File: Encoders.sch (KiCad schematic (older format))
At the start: 32 parts

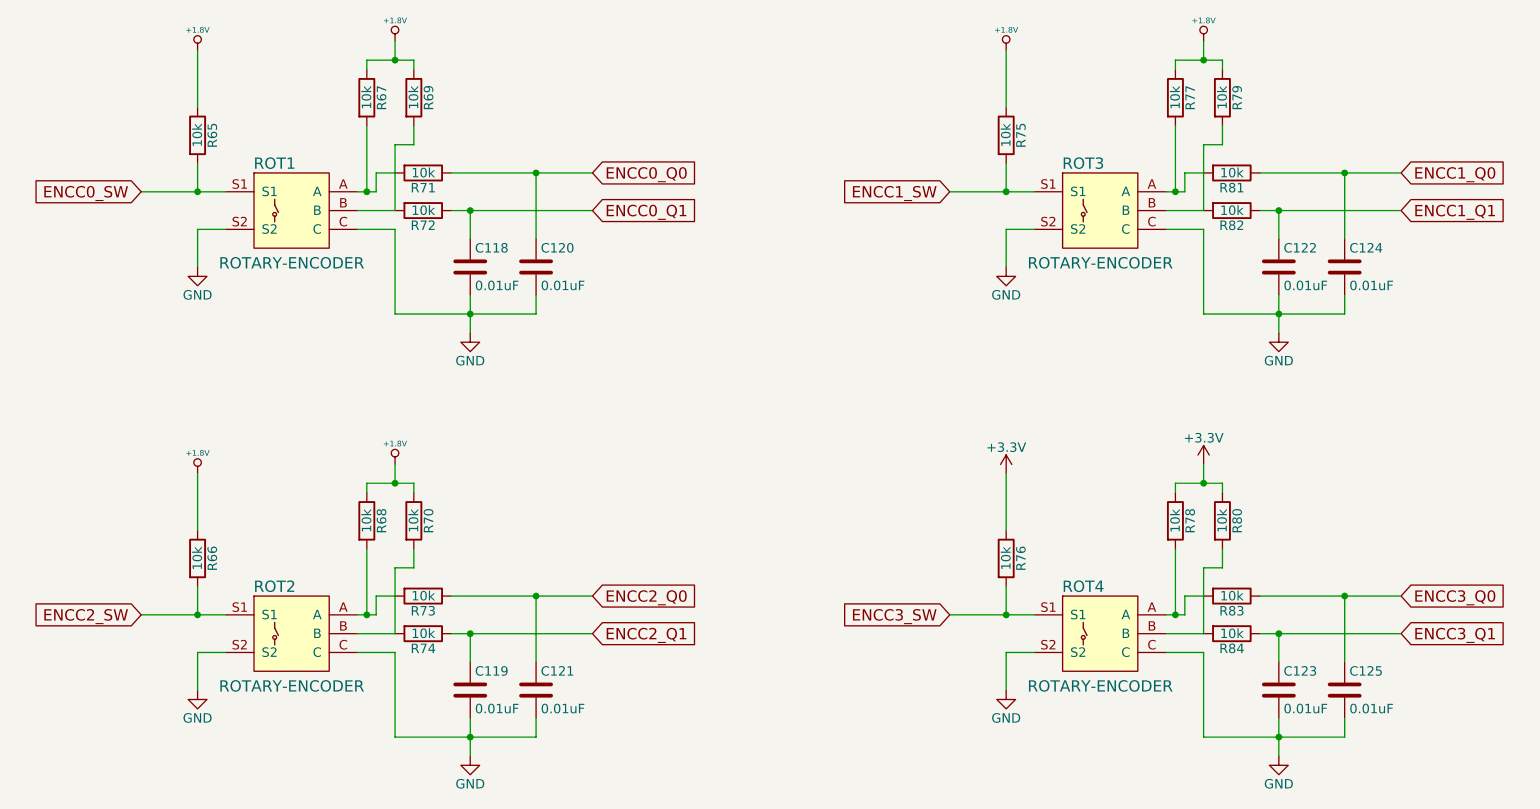
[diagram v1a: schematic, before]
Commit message: started PCBnew trivial connections and BGA interface, shuffled some net connections, etc.
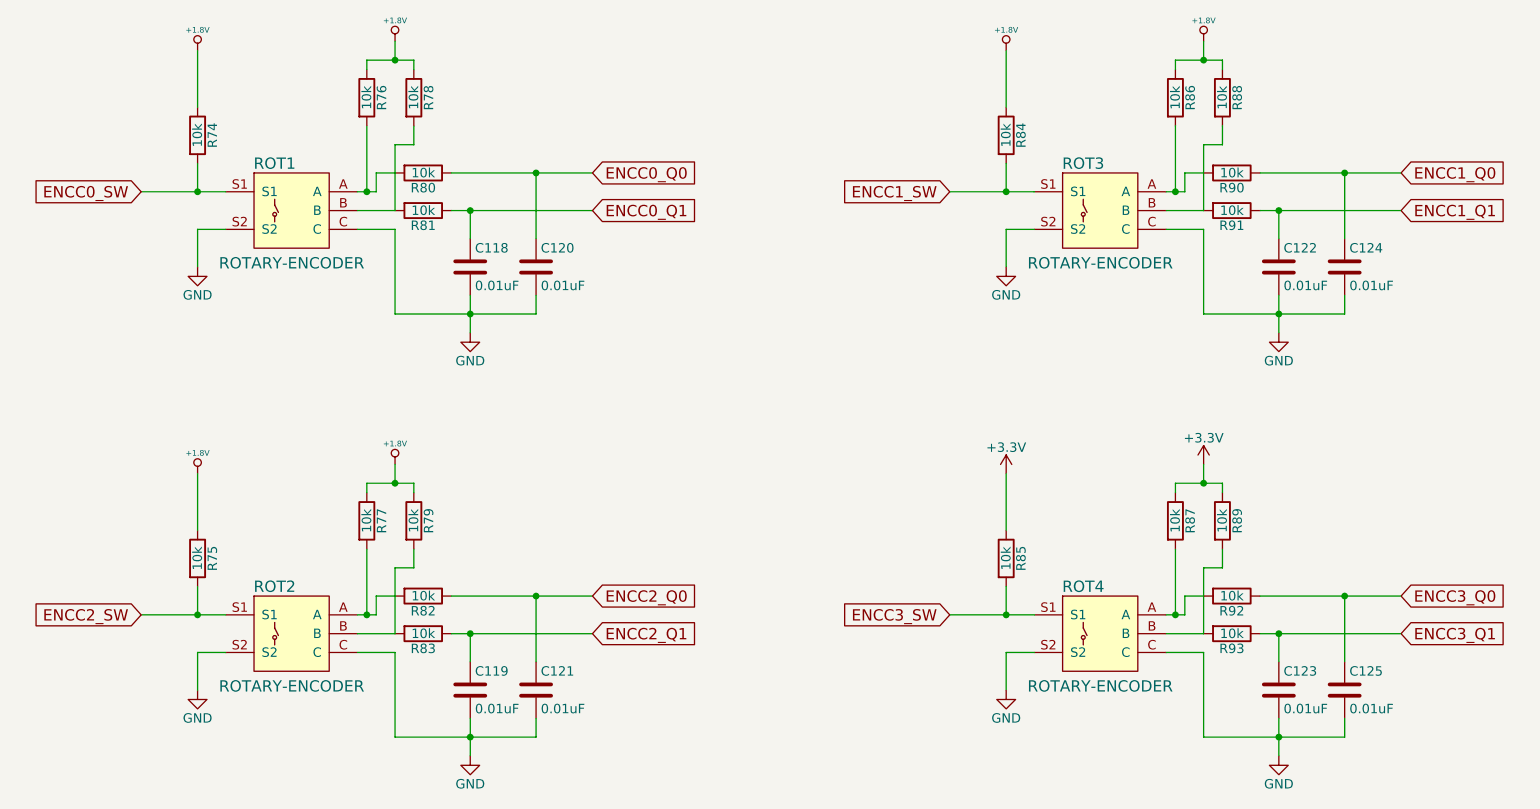
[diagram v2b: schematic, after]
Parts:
- renumbered R65 to R74, R66 to R75, R67 to R76, R68 to R77, R69 to R78, R70 to R79, R71 to R80, R72 to R81, R73 to R82, R74 to R83, R75 to R84, R76 to R85, R77 to R86, R78 to R87, R79 to R88, R80 to R89, R81 to R90, R82 to R91, R83 to R92, R84 to R93
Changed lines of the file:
@@
 LIBS:JACK_TRS_5PINS
 LIBS:MEMSMIC
+LIBS:illuminatedswitch
 EELAYER 25 0
 EELAYER END
@@
 $EndComp
 $Comp
-L R R72
+L R R81
 U 1 1 586C395E
 P 4150 2600
-F 0 "R72" V 4230 2600 50  0000 C CNN
+F 0 "R81" V 4230 2600 50  0000 C CNN
 F 1 "10k" V 4150 2600 50  0000 C CNN
 F 2 "Resistors_SMD:R_1206" V 4080 2600 50  0001 C CNN
@@
 $EndComp
 $Comp
-L R R71
+L R R80
 U 1 1 586C39C5
 P 4150 2400
-F 0 "R71" V 4230 2400 50  0000 C CNN
+F 0 "R80" V 4230 2400 50  0000 C CNN
 F 1 "10k" V 4150 2400 50  0000 C CNN
 F 2 "Resistors_SMD:R_1206" V 4080 2400 50  0001 C CNN
@@
 	4750 2400 4750 2750
 $Comp
-L R R67
+L R R76
 U 1 1 586C3A50
 P 3850 2000
-F 0 "R67" V 3930 2000 50  0000 C CNN
+F 0 "R76" V 3930 2000 50  0000 C CNN
 F 1 "10k" V 3850 2000 50  0000 C CNN
 F 2 "Resistors_SMD:R_1206" V 3780 2000 50  0001 C CNN
@@
 $EndComp
 $Comp
-L R R69
+L R R78
 U 1 1 586C3A87
 P 4100 2000
-F 0 "R69" V 4180 2000 50  0000 C CNN
+F 0 "R78" V 4180 2000 50  0000 C CNN
 F 1 "10k" V 4100 2000 50  0000 C CNN
 F 2 "Resistors_SMD:R_1206" V 4030 2000 50  0001 C CNN
@@
 Connection ~ 4000 1800
 $Comp
-L +1.8V #PWR0138
+L +1.8V #PWR0145
 U 1 1 586C41F4
 P 4000 1700
-F 0 "#PWR0138" H 4000 1840 20  0001 C CNN
+F 0 "#PWR0145" H 4000 1840 20  0001 C CNN
 F 1 "+1.8V" H 4000 1810 30  0000 C CNN
 F 2 "" H 4000 1700 60  0001 C CNN
@@
 $EndComp
 $Comp
-L GND #PWR0139
+L GND #PWR0146
 U 1 1 586C4216
 P 4400 3250
-F 0 "#PWR0139" H 4400 3000 50  0001 C CNN
+F 0 "#PWR0146" H 4400 3000 50  0001 C CNN
 F 1 "GND" H 4400 3100 50  0000 C CNN
 F 2 "" H 4400 3250 50  0000 C CNN
@@
 $EndComp
 $Comp
-L R R65
+L R R74
 U 1 1 586C42C6
 P 2950 2200
-F 0 "R65" V 3030 2200 50  0000 C CNN
+F 0 "R74" V 3030 2200 50  0000 C CNN
 F 1 "10k" V 2950 2200 50  0000 C CNN
 F 2 "Resistors_SMD:R_1206" V 2880 2200 50  0001 C CNN
@@
 	2950 2700 2950 2900
 $Comp
-L GND #PWR0140
+L GND #PWR0147
 U 1 1 586C437C
 P 2950 2900
-F 0 "#PWR0140" H 2950 2650 50  0001 C CNN
+F 0 "#PWR0147" H 2950 2650 50  0001 C CNN
 F 1 "GND" H 2950 2750 50  0000 C CNN
 F 2 "" H 2950 2900 50  0000 C CNN
@@
 $EndComp
 $Comp
-L +1.8V #PWR0141
+L +1.8V #PWR0148
 U 1 1 586C43A0
 P 2950 1750
-F 0 "#PWR0141" H 2950 1890 20  0001 C CNN
+F 0 "#PWR0148" H 2950 1890 20  0001 C CNN
 F 1 "+1.8V" H 2950 1860 30  0000 C CNN
 F 2 "" H 2950 1750 60  0001 C CNN
@@
 $EndComp
 $Comp
-L R R82
+L R R91
 U 1 1 586C5704
 P 8450 2600
-F 0 "R82" V 8530 2600 50  0000 C CNN
+F 0 "R91" V 8530 2600 50  0000 C CNN
 F 1 "10k" V 8450 2600 50  0000 C CNN
 F 2 "Resistors_SMD:R_1206" V 8380 2600 50  0001 C CNN
@@
 $EndComp
 $Comp
-L R R81
+L R R90
 U 1 1 586C570A
 P 8450 2400
-F 0 "R81" V 8530 2400 50  0000 C CNN
+F 0 "R90" V 8530 2400 50  0000 C CNN
 F 1 "10k" V 8450 2400 50  0000 C CNN
 F 2 "Resistors_SMD:R_1206" V 8380 2400 50  0001 C CNN
@@
 	9050 2400 9050 2750
 $Comp
-L R R77
+L R R86
 U 1 1 586C5718
 P 8150 2000
-F 0 "R77" V 8230 2000 50  0000 C CNN
+F 0 "R86" V 8230 2000 50  0000 C CNN
 F 1 "10k" V 8150 2000 50  0000 C CNN
 F 2 "Resistors_SMD:R_1206" V 8080 2000 50  0001 C CNN
@@
 $EndComp
 $Comp
-L R R79
+L R R88
 U 1 1 586C571E
 P 8400 2000
-F 0 "R79" V 8480 2000 50  0000 C CNN
+F 0 "R88" V 8480 2000 50  0000 C CNN
 F 1 "10k" V 8400 2000 50  0000 C CNN
 F 2 "Resistors_SMD:R_1206" V 8330 2000 50  0001 C CNN
@@
 Connection ~ 8300 1800
 $Comp
-L +1.8V #PWR0142
+L +1.8V #PWR0149
 U 1 1 586C5734
 P 8300 1700
-F 0 "#PWR0142" H 8300 1840 20  0001 C CNN
+F 0 "#PWR0149" H 8300 1840 20  0001 C CNN
 F 1 "+1.8V" H 8300 1810 30  0000 C CNN
 F 2 "" H 8300 1700 60  0001 C CNN
@@
 $EndComp
 $Comp
-L GND #PWR0143
+L GND #PWR0150
 U 1 1 586C573A
 P 8700 3250
-F 0 "#PWR0143" H 8700 3000 50  0001 C CNN
+F 0 "#PWR0150" H 8700 3000 50  0001 C CNN
 F 1 "GND" H 8700 3100 50  0000 C CNN
 F 2 "" H 8700 3250 50  0000 C CNN
@@
 $EndComp
 $Comp
-L R R75
+L R R84
 U 1 1 586C5740
 P 7250 2200
-F 0 "R75" V 7330 2200 50  0000 C CNN
+F 0 "R84" V 7330 2200 50  0000 C CNN
 F 1 "10k" V 7250 2200 50  0000 C CNN
 F 2 "Resistors_SMD:R_1206" V 7180 2200 50  0001 C CNN
@@
 	7250 2700 7250 2900
 $Comp
-L GND #PWR0144
+L GND #PWR0151
 U 1 1 586C5748
 P 7250 2900
-F 0 "#PWR0144" H 7250 2650 50  0001 C CNN
+F 0 "#PWR0151" H 7250 2650 50  0001 C CNN
 F 1 "GND" H 7250 2750 50  0000 C CNN
 F 2 "" H 7250 2900 50  0000 C CNN
@@
 $EndComp
 $Comp
-L +1.8V #PWR0145
+L +1.8V #PWR0152
 U 1 1 586C574E
 P 7250 1750
-F 0 "#PWR0145" H 7250 1890 20  0001 C CNN
+F 0 "#PWR0152" H 7250 1890 20  0001 C CNN
 F 1 "+1.8V" H 7250 1860 30  0000 C CNN
 F 2 "" H 7250 1750 60  0001 C CNN
@@
 $EndComp
 $Comp
-L R R74
+L R R83
 U 1 1 586C5B4F
 P 4150 4850
-F 0 "R74" V 4230 4850 50  0000 C CNN
+F 0 "R83" V 4230 4850 50  0000 C CNN
 F 1 "10k" V 4150 4850 50  0000 C CNN
 F 2 "Resistors_SMD:R_1206" V 4080 4850 50  0001 C CNN
@@
 $EndComp
 $Comp
-L R R73
+L R R82
 U 1 1 586C5B55
 P 4150 4650
-F 0 "R73" V 4230 4650 50  0000 C CNN
+F 0 "R82" V 4230 4650 50  0000 C CNN
 F 1 "10k" V 4150 4650 50  0000 C CNN
 F 2 "Resistors_SMD:R_1206" V 4080 4650 50  0001 C CNN
@@
 	4750 4650 4750 5000
 $Comp
-L R R68
+L R R77
 U 1 1 586C5B63
 P 3850 4250
-F 0 "R68" V 3930 4250 50  0000 C CNN
+F 0 "R77" V 3930 4250 50  0000 C CNN
 F 1 "10k" V 3850 4250 50  0000 C CNN
 F 2 "Resistors_SMD:R_1206" V 3780 4250 50  0001 C CNN
@@
 $EndComp
 $Comp
-L R R70
+L R R79
 U 1 1 586C5B69
 P 4100 4250
-F 0 "R70" V 4180 4250 50  0000 C CNN
+F 0 "R79" V 4180 4250 50  0000 C CNN
 F 1 "10k" V 4100 4250 50  0000 C CNN
 F 2 "Resistors_SMD:R_1206" V 4030 4250 50  0001 C CNN
@@
 Connection ~ 4000 4050
 $Comp
-L +1.8V #PWR0146
+L +1.8V #PWR0153
 U 1 1 586C5B7F
 P 4000 3950
-F 0 "#PWR0146" H 4000 4090 20  0001 C CNN
+F 0 "#PWR0153" H 4000 4090 20  0001 C CNN
 F 1 "+1.8V" H 4000 4060 30  0000 C CNN
 F 2 "" H 4000 3950 60  0001 C CNN
@@
 $EndComp
 $Comp
-L GND #PWR0147
+L GND #PWR0154
 U 1 1 586C5B85
 P 4400 5500
-F 0 "#PWR0147" H 4400 5250 50  0001 C CNN
+F 0 "#PWR0154" H 4400 5250 50  0001 C CNN
 F 1 "GND" H 4400 5350 50  0000 C CNN
 F 2 "" H 4400 5500 50  0000 C CNN
@@
 $EndComp
 $Comp
-L R R66
+L R R75
 U 1 1 586C5B8B
 P 2950 4450
-F 0 "R66" V 3030 4450 50  0000 C CNN
+F 0 "R75" V 3030 4450 50  0000 C CNN
 F 1 "10k" V 2950 4450 50  0000 C CNN
 F 2 "Resistors_SMD:R_1206" V 2880 4450 50  0001 C CNN
@@
 	2950 4950 2950 5150
 $Comp
-L GND #PWR0148
+L GND #PWR0155
 U 1 1 586C5B93
 P 2950 5150
-F 0 "#PWR0148" H 2950 4900 50  0001 C CNN
+F 0 "#PWR0155" H 2950 4900 50  0001 C CNN
 F 1 "GND" H 2950 5000 50  0000 C CNN
 F 2 "" H 2950 5150 50  0000 C CNN
@@
 $EndComp
 $Comp
-L +1.8V #PWR0149
+L +1.8V #PWR0156
 U 1 1 586C5B99
 P 2950 4000
-F 0 "#PWR0149" H 2950 4140 20  0001 C CNN
+F 0 "#PWR0156" H 2950 4140 20  0001 C CNN
 F 1 "+1.8V" H 2950 4110 30  0000 C CNN
 F 2 "" H 2950 4000 60  0001 C CNN
@@
 $EndComp
 $Comp
-L R R84
+L R R93
 U 1 1 586C626A
 P 8450 4850
-F 0 "R84" V 8530 4850 50  0000 C CNN
+F 0 "R93" V 8530 4850 50  0000 C CNN
 F 1 "10k" V 8450 4850 50  0000 C CNN
 F 2 "Resistors_SMD:R_1206" V 8380 4850 50  0001 C CNN
@@
 $EndComp
 $Comp
-L R R83
+L R R92
 U 1 1 586C6270
 P 8450 4650
-F 0 "R83" V 8530 4650 50  0000 C CNN
+F 0 "R92" V 8530 4650 50  0000 C CNN
 F 1 "10k" V 8450 4650 50  0000 C CNN
 F 2 "Resistors_SMD:R_1206" V 8380 4650 50  0001 C CNN
@@
 	9050 4650 9050 5000
 $Comp
-L R R78
+L R R87
 U 1 1 586C627E
 P 8150 4250
-F 0 "R78" V 8230 4250 50  0000 C CNN
+F 0 "R87" V 8230 4250 50  0000 C CNN
 F 1 "10k" V 8150 4250 50  0000 C CNN
 F 2 "Resistors_SMD:R_1206" V 8080 4250 50  0001 C CNN
@@
 $EndComp
 $Comp
-L R R80
+L R R89
 U 1 1 586C6284
 P 8400 4250
-F 0 "R80" V 8480 4250 50  0000 C CNN
+F 0 "R89" V 8480 4250 50  0000 C CNN
 F 1 "10k" V 8400 4250 50  0000 C CNN
 F 2 "Resistors_SMD:R_1206" V 8330 4250 50  0001 C CNN
@@
 Connection ~ 8300 4050
 $Comp
-L GND #PWR0150
+L GND #PWR0157
 U 1 1 586C62A0
 P 8700 5500
-F 0 "#PWR0150" H 8700 5250 50  0001 C CNN
+F 0 "#PWR0157" H 8700 5250 50  0001 C CNN
 F 1 "GND" H 8700 5350 50  0000 C CNN
 F 2 "" H 8700 5500 50  0000 C CNN
@@
 $EndComp
 $Comp
-L R R76
+L R R85
 U 1 1 586C62A6
 P 7250 4450
-F 0 "R76" V 7330 4450 50  0000 C CNN
+F 0 "R85" V 7330 4450 50  0000 C CNN
 F 1 "10k" V 7250 4450 50  0000 C CNN
 F 2 "Resistors_SMD:R_1206" V 7180 4450 50  0001 C CNN
@@
 	7250 4950 7250 5150
 $Comp
-L GND #PWR0151
+L GND #PWR0158
 U 1 1 586C62AE
 P 7250 5150
-F 0 "#PWR0151" H 7250 4900 50  0001 C CNN
+F 0 "#PWR0158" H 7250 4900 50  0001 C CNN
 F 1 "GND" H 7250 5000 50  0000 C CNN
 F 2 "" H 7250 5150 50  0000 C CNN
@@
 Connection ~ 7250 4750
 $Comp
-L +3.3V #PWR0152
+L +3.3V #PWR0159
 U 1 1 587428B8
 P 8300 3950
-F 0 "#PWR0152" H 8300 3800 50  0001 C CNN
+F 0 "#PWR0159" H 8300 3800 50  0001 C CNN
 F 1 "+3.3V" H 8300 4090 50  0000 C CNN
 F 2 "" H 8300 3950 50  0000 C CNN
@@
 $EndComp
 $Comp
-L +3.3V #PWR0153
+L +3.3V #PWR0160
 U 1 1 58742FBB
 P 7250 4000
-F 0 "#PWR0153" H 7250 3850 50  0001 C CNN
+F 0 "#PWR0160" H 7250 3850 50  0001 C CNN
 F 1 "+3.3V" H 7250 4140 50  0000 C CNN
 F 2 "" H 7250 4000 50  0000 C CNN

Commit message: annotate from scratch
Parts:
- renumbered C118 to C119, C119 to C120, C120 to C121, C121 to C122, C122 to C123, C123 to C124, C124 to C125, C125 to C126, R74 to R73, R75 to R74, R76 to R75, R77 to R76, R78 to R77, R79 to R78, R80 to R79, R81 to R80, R82 to R81, R83 to R82, R84 to R83, R85 to R84, R86 to R85, R87 to R86, R88 to R87, R89 to R88, R90 to R89, R91 to R90, R92 to R91, R93 to R92

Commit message: ran all FX3 BGA traces
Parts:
- renumbered C119 to C118, C120 to C119, C121 to C120, C122 to C121, C123 to C122, C124 to C123, C125 to C124, C126 to C125
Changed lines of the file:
@@
 $EndComp
 $Comp
-L C C119
+L C C118
 U 1 1 586C369D
 P 4400 2900
-F 0 "C119" H 4425 3000 50  0000 L CNN
+F 0 "C118" H 4425 3000 50  0000 L CNN
 F 1 "0.01uF" H 4425 2800 50  0000 L CNN
 F 2 "Capacitors_SMD:C_0402" H 4438 2750 50  0001 C CNN
@@
 $EndComp
 $Comp
-L C C121
+L C C120
 U 1 1 586C3858
 P 4750 2900
-F 0 "C121" H 4775 3000 50  0000 L CNN
+F 0 "C120" H 4775 3000 50  0000 L CNN
 F 1 "0.01uF" H 4775 2800 50  0000 L CNN
 F 2 "Capacitors_SMD:C_0402" H 4788 2750 50  0001 C CNN
@@
 Connection ~ 4000 1800
 $Comp
-L +1.8V #PWR149
+L +1.8V #PWR0147
 U 1 1 586C41F4
 P 4000 1700
-F 0 "#PWR149" H 4000 1840 20  0001 C CNN
+F 0 "#PWR0147" H 4000 1840 20  0001 C CNN
 F 1 "+1.8V" H 4000 1810 30  0000 C CNN
 F 2 "" H 4000 1700 60  0001 C CNN
@@
 $EndComp
 $Comp
-L GND #PWR151
+L GND #PWR0148
 U 1 1 586C4216
 P 4400 3250
-F 0 "#PWR151" H 4400 3000 50  0001 C CNN
+F 0 "#PWR0148" H 4400 3000 50  0001 C CNN
 F 1 "GND" H 4400 3100 50  0000 C CNN
 F 2 "" H 4400 3250 50  0000 C CNN
@@
 	2950 2700 2950 2900
 $Comp
-L GND #PWR146
+L GND #PWR0149
 U 1 1 586C437C
 P 2950 2900
-F 0 "#PWR146" H 2950 2650 50  0001 C CNN
+F 0 "#PWR0149" H 2950 2650 50  0001 C CNN
 F 1 "GND" H 2950 2750 50  0000 C CNN
 F 2 "" H 2950 2900 50  0000 C CNN
@@
 $EndComp
 $Comp
-L +1.8V #PWR145
+L +1.8V #PWR0150
 U 1 1 586C43A0
 P 2950 1750
-F 0 "#PWR145" H 2950 1890 20  0001 C CNN
+F 0 "#PWR0150" H 2950 1890 20  0001 C CNN
 F 1 "+1.8V" H 2950 1860 30  0000 C CNN
 F 2 "" H 2950 1750 60  0001 C CNN
@@
 $EndComp
 $Comp
-L C C123
+L C C122
 U 1 1 586C56F8
 P 8700 2900
-F 0 "C123" H 8725 3000 50  0000 L CNN
+F 0 "C122" H 8725 3000 50  0000 L CNN
 F 1 "0.01uF" H 8725 2800 50  0000 L CNN
 F 2 "Capacitors_SMD:C_0402" H 8738 2750 50  0001 C CNN
@@
 $EndComp
 $Comp
-L C C125
+L C C124
 U 1 1 586C56FE
 P 9050 2900
-F 0 "C125" H 9075 3000 50  0000 L CNN
+F 0 "C124" H 9075 3000 50  0000 L CNN
 F 1 "0.01uF" H 9075 2800 50  0000 L CNN
 F 2 "Capacitors_SMD:C_0402" H 9088 2750 50  0001 C CNN
@@
 Connection ~ 8300 1800
 $Comp
-L +1.8V #PWR157
+L +1.8V #PWR0151
 U 1 1 586C5734
 P 8300 1700
-F 0 "#PWR157" H 8300 1840 20  0001 C CNN
+F 0 "#PWR0151" H 8300 1840 20  0001 C CNN
 F 1 "+1.8V" H 8300 1810 30  0000 C CNN
 F 2 "" H 8300 1700 60  0001 C CNN
@@
 $EndComp
 $Comp
-L GND #PWR159
+L GND #PWR0152
 U 1 1 586C573A
 P 8700 3250
-F 0 "#PWR159" H 8700 3000 50  0001 C CNN
+F 0 "#PWR0152" H 8700 3000 50  0001 C CNN
 F 1 "GND" H 8700 3100 50  0000 C CNN
 F 2 "" H 8700 3250 50  0000 C CNN
@@
 	7250 2700 7250 2900
 $Comp
-L GND #PWR154
+L GND #PWR0153
 U 1 1 586C5748
 P 7250 2900
-F 0 "#PWR154" H 7250 2650 50  0001 C CNN
+F 0 "#PWR0153" H 7250 2650 50  0001 C CNN
 F 1 "GND" H 7250 2750 50  0000 C CNN
 F 2 "" H 7250 2900 50  0000 C CNN
@@
 $EndComp
 $Comp
-L +1.8V #PWR153
+L +1.8V #PWR0154
 U 1 1 586C574E
 P 7250 1750
-F 0 "#PWR153" H 7250 1890 20  0001 C CNN
+F 0 "#PWR0154" H 7250 1890 20  0001 C CNN
 F 1 "+1.8V" H 7250 1860 30  0000 C CNN
 F 2 "" H 7250 1750 60  0001 C CNN
@@
 $EndComp
 $Comp
-L C C120
+L C C119
 U 1 1 586C5B43
 P 4400 5150
-F 0 "C120" H 4425 5250 50  0000 L CNN
+F 0 "C119" H 4425 5250 50  0000 L CNN
 F 1 "0.01uF" H 4425 5050 50  0000 L CNN
 F 2 "Capacitors_SMD:C_0402" H 4438 5000 50  0001 C CNN
@@
 $EndComp
 $Comp
-L C C122
+L C C121
 U 1 1 586C5B49
 P 4750 5150
-F 0 "C122" H 4775 5250 50  0000 L CNN
+F 0 "C121" H 4775 5250 50  0000 L CNN
 F 1 "0.01uF" H 4775 5050 50  0000 L CNN
 F 2 "Capacitors_SMD:C_0402" H 4788 5000 50  0001 C CNN
@@
 Connection ~ 4000 4050
 $Comp
-L +1.8V #PWR150
+L +1.8V #PWR0155
 U 1 1 586C5B7F
 P 4000 3950
-F 0 "#PWR150" H 4000 4090 20  0001 C CNN
+F 0 "#PWR0155" H 4000 4090 20  0001 C CNN
 F 1 "+1.8V" H 4000 4060 30  0000 C CNN
 F 2 "" H 4000 3950 60  0001 C CNN
@@
 $EndComp
 $Comp
-L GND #PWR152
+L GND #PWR0156
 U 1 1 586C5B85
 P 4400 5500
-F 0 "#PWR152" H 4400 5250 50  0001 C CNN
+F 0 "#PWR0156" H 4400 5250 50  0001 C CNN
 F 1 "GND" H 4400 5350 50  0000 C CNN
 F 2 "" H 4400 5500 50  0000 C CNN
@@
 	2950 4950 2950 5150
 $Comp
-L GND #PWR148
+L GND #PWR0157
 U 1 1 586C5B93
 P 2950 5150
-F 0 "#PWR148" H 2950 4900 50  0001 C CNN
+F 0 "#PWR0157" H 2950 4900 50  0001 C CNN
 F 1 "GND" H 2950 5000 50  0000 C CNN
 F 2 "" H 2950 5150 50  0000 C CNN
@@
 $EndComp
 $Comp
-L +1.8V #PWR147
+L +1.8V #PWR0158
 U 1 1 586C5B99
 P 2950 4000
-F 0 "#PWR147" H 2950 4140 20  0001 C CNN
+F 0 "#PWR0158" H 2950 4140 20  0001 C CNN
 F 1 "+1.8V" H 2950 4110 30  0000 C CNN
 F 2 "" H 2950 4000 60  0001 C CNN
@@
 $EndComp
 $Comp
-L C C124
+L C C123
 U 1 1 586C625E
 P 8700 5150
-F 0 "C124" H 8725 5250 50  0000 L CNN
+F 0 "C123" H 8725 5250 50  0000 L CNN
 F 1 "0.01uF" H 8725 5050 50  0000 L CNN
 F 2 "Capacitors_SMD:C_0402" H 8738 5000 50  0001 C CNN
@@
 $EndComp
 $Comp
-L C C126
+L C C125
 U 1 1 586C6264
 P 9050 5150
-F 0 "C126" H 9075 5250 50  0000 L CNN
+F 0 "C125" H 9075 5250 50  0000 L CNN
 F 1 "0.01uF" H 9075 5050 50  0000 L CNN
 F 2 "Capacitors_SMD:C_0402" H 9088 5000 50  0001 C CNN
@@
 Connection ~ 8300 4050
 $Comp
-L GND #PWR160
+L GND #PWR0159
 U 1 1 586C62A0
 P 8700 5500
-F 0 "#PWR160" H 8700 5250 50  0001 C CNN
+F 0 "#PWR0159" H 8700 5250 50  0001 C CNN
 F 1 "GND" H 8700 5350 50  0000 C CNN
 F 2 "" H 8700 5500 50  0000 C CNN
@@
 	7250 4950 7250 5150
 $Comp
-L GND #PWR156
+L GND #PWR0160
 U 1 1 586C62AE
 P 7250 5150
-F 0 "#PWR156" H 7250 4900 50  0001 C CNN
+F 0 "#PWR0160" H 7250 4900 50  0001 C CNN
 F 1 "GND" H 7250 5000 50  0000 C CNN
 F 2 "" H 7250 5150 50  0000 C CNN
@@
 Connection ~ 7250 4750
 $Comp
-L +3.3V #PWR158
+L +3.3V #PWR0161
 U 1 1 587428B8
 P 8300 3950
-F 0 "#PWR158" H 8300 3800 50  0001 C CNN
+F 0 "#PWR0161" H 8300 3800 50  0001 C CNN
 F 1 "+3.3V" H 8300 4090 50  0000 C CNN
 F 2 "" H 8300 3950 50  0000 C CNN
@@
 $EndComp
 $Comp
-L +3.3V #PWR155
+L +3.3V #PWR0162
 U 1 1 58742FBB
 P 7250 4000
-F 0 "#PWR155" H 7250 3850 50  0001 C CNN
+F 0 "#PWR0162" H 7250 3850 50  0001 C CNN
 F 1 "+3.3V" H 7250 4140 50  0000 C CNN
 F 2 "" H 7250 4000 50  0000 C CNN
